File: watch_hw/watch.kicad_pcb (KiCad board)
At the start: 4 copper layers, 39 x 39.6 mm, 78 parts, among them J1 USB_C_Receptacle_USB2.0, M1 VZ43FC1B5640005L, Q1 DMN65D8LFB, Q2 SSM6J501NU, SW1 TL6340AF160Q, SW2 TL6340AF160Q, U1 BLUENRG-LPS, U2 FT234XD-R, U3 MAX17048G+, U4 LTC3130EUDC-1#PBF, U5 MCP73831-2ACI/MC, U6 MAXM86161EFD+T, U7 BMA456, Y1 Crystal_Small, Y2 Crystal_Small

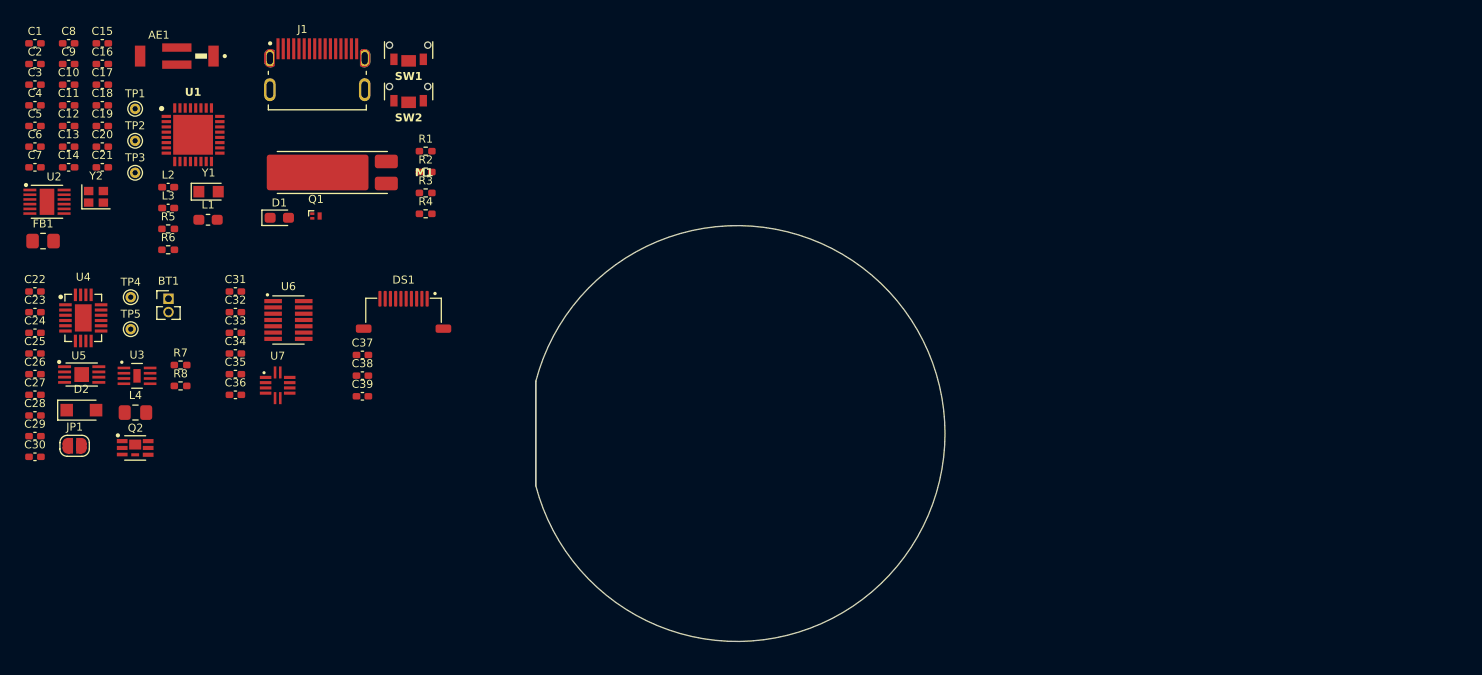
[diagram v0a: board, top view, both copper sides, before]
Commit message: Finalize (?) part selection, start layout
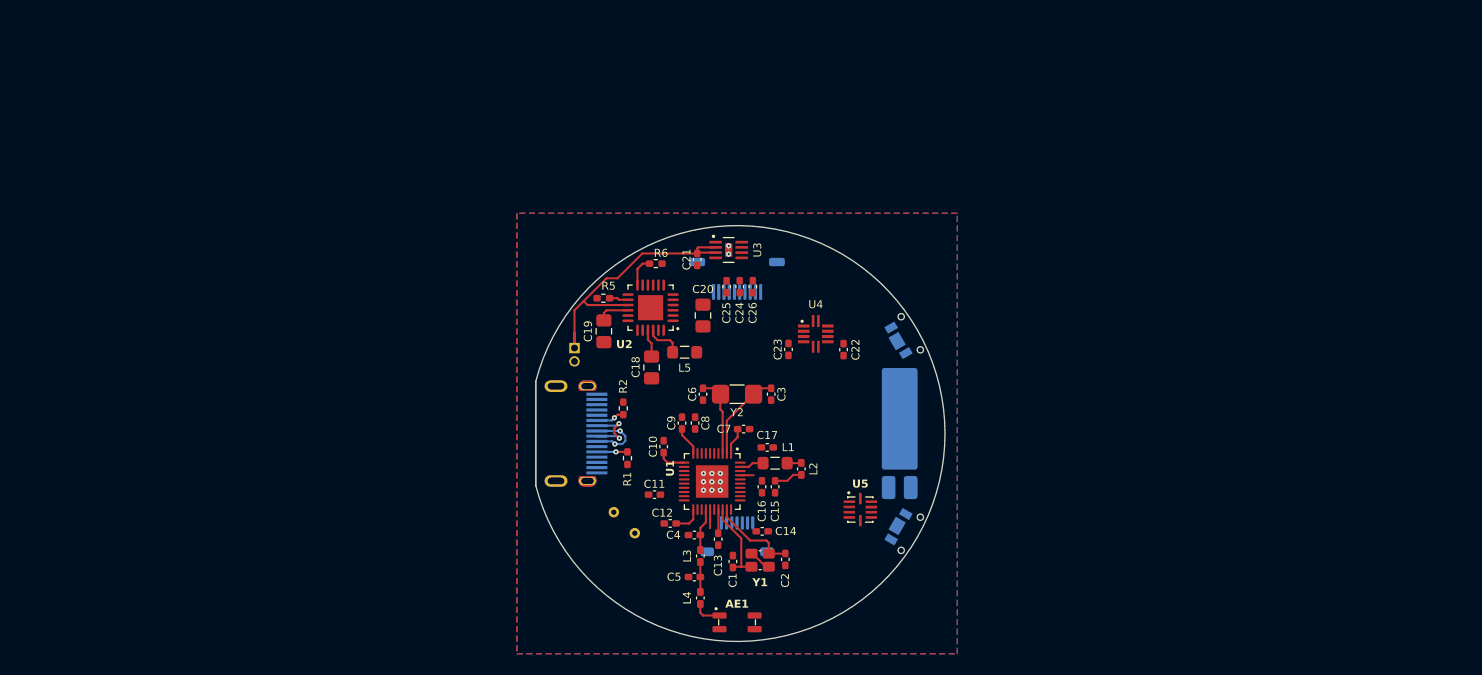
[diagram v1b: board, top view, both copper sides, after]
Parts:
- removed C27: 33u, Capacitor_SMD:C_0402_1005Metric_Pad0.74x0.62mm_HandSolder
- removed C28, C29, C30: 4.7u, Capacitor_SMD:C_0402_1005Metric_Pad0.74x0.62mm_HandSolder
- removed C31: 10u, Capacitor_SMD:C_0402_1005Metric_Pad0.74x0.62mm_HandSolder
- removed C32, C34, C35, C39: 0.1u, Capacitor_SMD:C_0402_1005Metric_Pad0.74x0.62mm_HandSolder
- removed C33, C36, C37, C38: 1u, Capacitor_SMD:C_0402_1005Metric_Pad0.74x0.62mm_HandSolder
- removed D1: D, Diode_SMD:D_0603_1608Metric_Pad1.05x0.95mm_HandSolder
- removed D2: PMEG10020AELR, Diode_SMD:Nexperia_CFP3_SOD-123W
- removed FB1: MI0805K601R-10, Resistor_SMD:R_0805_2012Metric_Pad1.20x1.40mm_HandSolder
- removed JP1: SolderJumper_2_Open, Jumper:SolderJumper-2_P1.3mm_Open_RoundedPad1.0x1.5mm
- removed Q1: DMN65D8LFB, Package_DFN_QFN:Diodes_DFN1006-3
- removed Q2: SSM6J501NU, watch:TRANS_SSM6J501NU,LF
- removed R3: 220, Resistor_SMD:R_0402_1005Metric_Pad0.72x0.64mm_HandSolder
- removed R4, R7: 10k, Resistor_SMD:R_0402_1005Metric_Pad0.72x0.64mm_HandSolder
- removed R8: 5k, Resistor_SMD:R_0402_1005Metric_Pad0.72x0.64mm_HandSolder
- removed TP3: SWDIO, TestPoint:TestPoint_THTPad_D1.0mm_Drill0.5mm
- removed TP4: VDD, TestPoint:TestPoint_THTPad_D1.0mm_Drill0.5mm
- removed TP5: PGOOD, TestPoint:TestPoint_THTPad_D1.0mm_Drill0.5mm
- removed U6: MAXM86161EFD+T, watch:MAXM86161EFDT
- removed U7: BMA456, watch:XDCR_BMA456
- added J2: FH19C-7S-0.5SH, watch:FH19C-7S-0.5SH, B.Cu at (140.0, 110.0)
- added L5: 2.2uH, Inductor_SMD:L_0805_2012Metric_Pad1.05x1.20mm_HandSolder, F.Cu at (135.0, 92.2)
- AE1: value 2450AT43B100E -> 2450AT18D0100001; footprint watch:ANTENNA_2450AT43B100E -> watch:ANTENNA_2450AT18D0100001
- BT1: value Battery_Cell -> 402530; moved to B.Cu
- C1, C2: value 200nF -> 9pF
- C11: value 4.7uF -> 100nF
- C12: value 100nF -> 820pF
- C13: value 10nF -> 100pF
- C14: value 47pF -> 100nF
- C15: value 47pF -> 1uF
- C16: value 100nF -> 47nF
- C17: value 8.2pF -> 1uF
- C18, C19, C20: value 8.2pF -> 10uF; footprint Capacitor_SMD:C_0402_1005Metric_Pad0.74x0.62mm_HandSolder -> Capacitor_SMD:C_0805_2012Metric_Pad1.18x1.45mm_HandSolder
- C21: value 8.2pF -> 0.1u
- C23: value 22n -> 0.1u
- C24: value 22n -> 1u
- C25: value 47u -> 1u
- C26: value 1uF -> 0.1u
- C3, C6: value 200nF -> 10pF
- C4: value 200nF -> 1pF
- C5: value 200nF -> 1.2pF
- C7: value 200nF -> 100nF
- C8: value 200nF -> 4.7uF
- C9: value 100nF -> 4.7uF
- DS1, J1, M1, SW1, SW2: moved to B.Cu
- L1: footprint Inductor_SMD:L_0603_1608Metric_Pad1.05x0.95mm_HandSolder -> Inductor_SMD:L_0805_2012Metric_Pad1.05x1.20mm_HandSolder
- L2: value 22nH -> 15nH
- L3: value 22nH -> 4.7nF
- L4: value 4.7u -> 2.2nH; footprint Inductor_SMD:L_0805_2012Metric_Pad1.15x1.40mm_HandSolder -> Inductor_SMD:L_0402_1005Metric_Pad0.77x0.64mm_HandSolder
- R5: value 27R -> 10k
- R6: value 27R -> 560R
- TP1: value ~{RESET} -> SWDCLK; moved to B.Cu
- TP2: value SWDCLK -> SWDIO; moved to B.Cu
- U1: value BLUENRG-LPS -> NRF52833-QDAA; footprint watch:BLUERNG-332 -> watch:nRF52833-QD
- U2: value FT234XD-R -> nPM1100-QD; footprint watch:SON45P300X300X80-13N -> watch:nPM1100-QD
- U4: value LTC3130EUDC-1#PBF -> BMA456; footprint watch:QFN50P300X400X80-21M-D -> watch:XDCR_BMA456
- U5: value MCP73831-2ACI/MC -> DRV2603; footprint watch:SON50P200X300X100-9N -> watch:DRV2603RUN
- Y1: value Crystal_Small -> 32MHz; footprint Crystal:Crystal_SMD_2012-2Pin_2.0x1.2mm_HandSoldering -> watch:XTAL_ECX-1637B2
- Y2: value Crystal_Small -> 32.768kHz; footprint Crystal:Crystal_SMD_2016-4Pin_2.0x1.6mm -> watch:XTAL_SC32S
- moved C2 85.7 mm to (144.6, 112.0), turned to 90 degrees
- moved C1 82.9 mm to (139.6, 112.2), turned to -90 degrees
- moved C22 77.3 mm to (150.1, 92.0), turned to -90 degrees
- moved C15 76.8 mm to (143.6, 105.1), turned to -90 degrees
- moved C5 76.2 mm to (135.9, 113.7), turned to 180 degrees
- moved C3 76.1 mm to (143.2, 96.2), turned to 90 degrees
- moved AE1 75.9 mm to (140.0, 118.0)
- moved U5 75.3 mm to (151.7, 107.2)
- moved C4 75.0 mm to (135.9, 109.7), turned to 180 degrees
- moved C16 74.7 mm to (142.3, 105.1), turned to -90 degrees
- moved C14 74.7 mm to (142.4, 109.3)
- moved C13 72.4 mm to (138.2, 110.1), turned to -90 degrees
- moved C17 72.2 mm to (142.8, 101.3)
- moved C7 72.0 mm to (140.6, 99.6)
- moved C23 71.9 mm to (144.9, 92.0), turned to -90 degrees
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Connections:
- net /BLUENRG/DISP_INVERT renamed /Display/INVERT
- net /BLUENRG/DISP_SCLK renamed /Display/SCLK
- net /BLUENRG/DISP_SDO renamed /Display/SDI
- net /BLUENRG/TXD renamed /Power/BAT_ERR
- net /BLUENRG/~{BAT_ALRT} renamed /Power/~{BAT_ALRT}
- net /BLUENRG/~{CTS} renamed /Power/BAT_CHG
- AE1 pad 1: Net-(AE1-A) -> Net-(AE1-FEED)
- AE1 pad 2: (no net) -> GND
- C1 pad 1: VDD -> GND
- C1 pad 2: GND -> Net-(U1-XC1)
- C10 pad 1: Net-(U1-VFBSD) -> /SoC/DECUSB
- C11 pad 1: Net-(U2-VCC) -> VDD
- C12 pad 1: Net-(U2-VCC) -> /SoC/DEC5
- C13 pad 1: VBUS -> /SoC/DEC3
- C14 pad 1: GND -> VDD
- C14 pad 2: /BLUENRG/D_P -> GND
- C15 pad 1: GND -> /SoC/DEC6
- C15 pad 2: /BLUENRG/D_N -> GND
- C16 pad 1: /BLUENRG/USB_3V3 -> /SoC/DEC6
- C17 pad 1: Net-(U1-AT3/PB12/XTALO) -> VDD
- C18 pad 1: Net-(U1-AT2/PB13/XTALI) -> Net-(U2-DEC)
- C19 pad 1: Net-(U1-RF1) -> /Power/VSYS
- C19 pad 2: Net-(AE1-A) -> GND
- C2 pad 1: VDD -> GND
- C2 pad 2: GND -> Net-(U1-XC2)
- C20 pad 1: Net-(U1-RF1) -> VDD
- C21 pad 1: Net-(AE1-A) -> /Power/VBAT
- C22 pad 1: /Power/VBAT -> VDD
- C23 pad 1: Net-(U4-SW1) -> VDD
- C23 pad 2: Net-(U4-BST1) -> GND
- C24 pad 1: Net-(U4-BST2) -> VDD
- C24 pad 2: Net-(U4-SW2) -> GND
- C25 pad 1: Net-(D2-K) -> VDD
- C26 pad 1: Net-(D2-K) -> /Display/DISP_ON
- C3 pad 1: VDD -> GND
- C3 pad 2: GND -> Net-(U1-P0.00/XL1)
- C4 pad 1: VDD -> Net-(U1-ANT)
- C5 pad 1: VDD -> Net-(C5-Pad1)
- C6 pad 1: VDD -> GND
- C6 pad 2: GND -> Net-(U1-P0.01/XL2)
- C7 pad 1: /BLUENRG/VCAP -> /SoC/DEC1
- C9 pad 1: Net-(U1-VFBSD) -> VBUS
- DS1 pad 5: /BLUENRG/DISP_ON -> /Display/DISP_ON
- J1 pad A6: /BLUENRG/D_P -> /USB_D_P
- J1 pad A7: /BLUENRG/D_N -> /USB_D_N
- J1 pad B6: /BLUENRG/D_P -> /USB_D_P
- J1 pad B7: /BLUENRG/D_N -> /USB_D_N
- L1 pad 1: Net-(U1-VFBSD) -> Net-(U1-DCC)
- L2 pad 2: Net-(U1-VLXSD) -> /SoC/DEC6
- L3 pad 1: Net-(U1-RF1) -> Net-(U1-ANT)
- L3 pad 2: Net-(AE1-A) -> Net-(C5-Pad1)
- L4 pad 1: Net-(U4-SW1) -> Net-(C5-Pad1)
- L4 pad 2: Net-(U4-SW2) -> Net-(AE1-FEED)
- M1 pad 1: VDD -> Net-(M1-+)
- M1 pad 2: Net-(D1-A) -> Net-(M1--)
- R5 pad 1: Net-(U2-USBDM) -> GND
- R5 pad 2: /BLUENRG/D_N -> Net-(U2-NTC)
- R6 pad 1: Net-(U2-USBDP) -> GND
- R6 pad 2: /BLUENRG/D_P -> Net-(U2-ICHG)
- TP1 pad 1: Net-(U1-RSTN) -> Net-(U1-SWDCLK)
- TP2 pad 1: Net-(U1-PA3) -> Net-(U1-SWDIO)
- U1 pad 1: unconnected-(U1-PB3-Pad1) -> /SoC/DEC1
- U1 pad 10: unconnected-(U1-PA9-Pad10) -> VBUS
- U1 pad 11: unconnected-(U1-PA10-Pad11) -> /SoC/DECUSB
- U1 pad 12: unconnected-(U1-PA11-Pad12) -> /USB_D_N
- U1 pad 13: VDD -> /USB_D_P
- U1 pad 14: Net-(U1-RF1) -> unconnected-(U1-P0.15-Pad14)
- U1 pad 15: VDD -> unconnected-(U1-P0.17-Pad15)
- U1 pad 16: Net-(U1-OSCOUT) -> unconnected-(U1-P0.18/~{RESET}-Pad16)
- U1 pad 17: Net-(U1-OSCIN) -> unconnected-(U1-P0.20-Pad17)
- U1 pad 18: unconnected-(U1-AT0/PB15-Pad18) -> VDD
- U1 pad 19: unconnected-(U1-AT1/PB14-Pad19) -> Net-(U1-SWDIO)
- U1 pad 2: unconnected-(U1-PB2-Pad2) -> Net-(U1-P0.00/XL1)
- U1 pad 20: Net-(U1-AT2/PB13/XTALI) -> Net-(U1-SWDCLK)
- U1 pad 21: Net-(U1-AT3/PB12/XTALO) -> /SoC/DEC5
- U1 pad 24: VDD -> Net-(U1-ANT)
- U1 pad 25: Net-(U1-VLXSD) -> GND
- U1 pad 26: GND -> /SoC/DEC6
- U1 pad 27: Net-(U1-VFBSD) -> /SoC/DEC3
- U1 pad 28: /BLUENRG/VCAP -> Net-(U1-XC1)
- U1 pad 29: Net-(U1-RSTN) -> Net-(U1-XC2)
- U1 pad 3: unconnected-(U1-PB1-Pad3) -> Net-(U1-P0.01/XL2)
- U1 pad 30: unconnected-(U1-PB5-Pad30) -> VDD
- U1 pad 32: VDD -> unconnected-(U1-P0.02/AIN0-Pad32)
- U1 pad 33: GND -> unconnected-(U1-P0.28/AIN4-Pad33)
- U1 pad 5: Net-(U1-PA3) -> unconnected-(U1-P0.05/AIN3-Pad5)
- U1 pad 6: Net-(U1-PA2) -> unconnected-(U1-P1.09-Pad6)
- U1 pad 8: unconnected-(U1-PA0-Pad8) -> VDD
- U1 pad 9: unconnected-(U1-PA8-Pad9) -> VDD
- U2 pad 1: Net-(U2-USBDM) -> VDD
- U2 pad 11: /BLUENRG/~{RTS} -> GND
- U2 pad 12: Net-(U2-USBDP) -> Net-(U2-ICHG)
- U2 pad 13: GND -> unconnected-(U2-NC-Pad13)
- U2 pad 2: /BLUENRG/USB_3V3 -> /Power/VSYS
- U2 pad 3: /BLUENRG/USB_3V3 -> /Power/VSYS
- U2 pad 4: Net-(U2-VCC) -> unconnected-(U2-NC-Pad4)
- U2 pad 5: GND -> /Power/VSYS
- U2 pad 6: unconnected-(U2-CBUS0-Pad6) -> GND
- U2 pad 7: /BLUENRG/RXD -> GND
- U2 pad 9: /BLUENRG/USB_3V3 -> /Power/VSYS
- U4 pad 1: Net-(U4-BST1) -> GND
- U4 pad 10: /Power/BOOST_VCC -> VDD
- U4 pad 11: GND -> unconnected-(U4-ASCL-Pad11)
- U4 pad 12: Net-(JP1-A) -> /SCL
- U4 pad 2: Net-(D2-K) -> /SDA
- U4 pad 3: Net-(D2-K) -> VDD
- U4 pad 4: Net-(D2-K) -> unconnected-(U4-ASDA-Pad4)
- U4 pad 5: /Power/BOOST_VCC -> /Sensors/ACC_INT1
- U4 pad 6: /Power/BOOST_VCC -> /Sensors/ACC_INT2
- U4 pad 7: GND -> VDD
- U5 pad 1: VBUS -> /MOTOR_EN
- U5 pad 2: VBUS -> /MOTOR_PWM
- U5 pad 3: /Power/VBAT -> GND
- U5 pad 4: /Power/VBAT -> (no net)
- U5 pad 5: /Power/STAT -> GND
- U5 pad 6: GND -> Net-(M1--)
- U5 pad 7: (no net) -> VDD
- U5 pad 8: Net-(U5-PROG) -> GND
- U5 pad 9: GND -> Net-(M1-+)
- Y1 pad 1: Net-(U1-AT2/PB13/XTALI) -> Net-(U1-XC1)
- Y1 pad 2: Net-(U1-AT3/PB12/XTALO) -> GND
- Y2 pad 1: Net-(U1-OSCOUT) -> Net-(U1-P0.01/XL2)
- Y2 pad 2: Net-(U1-OSCIN) -> Net-(U1-P0.00/XL1)
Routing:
- net /Power/VBAT: track 0.00 -> 27.6 mm
- net Net-(U1-P0.00/XL1): track 0.00 -> 8.63 mm
- net Net-(U1-XC2): track 0.00 -> 8.35 mm
- net Net-(U1-XC1): track 0.00 -> 7.99 mm
- net Net-(U1-P0.01/XL2): track 0.00 -> 7.66 mm
- net /USB_D_P: track 0.00 -> 6.32 mm, vias 0 -> 2
- net /USB_D_N: track 0.00 -> 6.18 mm, vias 0 -> 2
- net GND: track 0.00 -> 5.20 mm, vias 0 -> 11
- net Net-(U1-ANT): track 0.00 -> 4.07 mm
- net Net-(U2-SW): track 0.00 -> 3.56 mm
- net /Power/VSYS: track 0.00 -> 3.12 mm
- net Net-(J1-CC1): track 0.00 -> 2.91 mm, vias 0 -> 1
- net Net-(U2-ICHG): track 0.00 -> 2.91 mm
- net Net-(C5-Pad1): track 0.00 -> 2.86 mm
- net VBUS: track 0.00 -> 2.78 mm
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- added copper zone on B.Cu, net GND
- added copper zone on F.Cu, net GND
- added copper zone on In1.Cu, net GND
- added copper zone on In4.Cu, net GND
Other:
- copper layers 4 -> 6

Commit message: Routing progress
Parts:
- added TP3: RESET, TestPoint:TestPoint_THTPad_D1.0mm_Drill0.5mm, B.Cu at (127.8, 106.2)
- C26: value 0.1u -> 0.1uF
- DS1: moved to F.Cu
- moved C26 25.1 mm to (154.3, 107.6), turned to -90 degrees
- moved DS1 22.8 mm to (155.8, 100.0), turned to 90 degrees
- moved C25 18.3 mm to (149.4, 101.0), turned to 180 degrees
- moved C24 16.5 mm to (149.4, 99.8), turned to 180 degrees
- moved AE1 13.7 mm to (127.5, 112.5), turned to 135 degrees
- moved J2 7.00 mm to (140.0, 117.0)
- moved L4 2.78 mm to (134.5, 113.8), turned to 180 degrees
- moved C15 2.67 mm to (146.2, 105.8)
- moved C16 2.67 mm to (144.9, 105.8)
- moved C14 1.64 mm to (142.6, 107.7)
- moved C1 1.60 mm to (139.4, 110.6)
- moved C2 1.58 mm to (144.4, 110.4)
- moved Y1 1.58 mm to (142.0, 110.5)
- moved TP2 1.25 mm to (129.2, 108.2)
- moved C13 1.18 mm to (138.2, 111.2)
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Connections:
- C26 pad 1: /Display/DISP_ON -> VDD
- DS1 pad 3: VDD -> /Display/DISP_CS
- DS1 pad 4: /Display/INVERT -> GND
- DS1 pad 5: /Display/DISP_ON -> VDD
- DS1 pad 8: unconnected-(DS1-EXTMODE-Pad8) -> GND
- J2 pad 3: /Sensors/HR_GPIO -> unconnected-(J2-Pin_3-Pad3)
- J2 pad 4: /Sensors/HR_LDO_EN -> unconnected-(J2-Pin_4-Pad4)
- U1 pad 16: unconnected-(U1-P0.18/~{RESET}-Pad16) -> Net-(U1-P0.18/~{RESET})
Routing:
- net VDD: track 0.00 -> 33.8 mm, vias 0 -> 11
- net /USB_D_P: track 6.32 -> 23.4 mm
- net /USB_D_N: track 6.18 -> 22.5 mm
- net GND: track 5.20 -> 14.8 mm, vias 11 -> 18
- net Net-(U1-P0.18/~{RESET}): track 0.00 -> 7.71 mm
- net Net-(U1-SWDIO): track 0.00 -> 6.64 mm
- net Net-(M1--): track 0.00 -> 6.45 mm, vias 0 -> 1
- net Net-(U1-SWDCLK): track 0.00 -> 6.05 mm
- net /Power/VSYS: track 3.12 -> 6.92 mm, vias 0 -> 5
- net /SoC/DEC6: track 2.73 -> 5.28 mm, vias 0 -> 2
- net /Power/VBAT: track 27.6 -> 25.3 mm
- net Net-(AE1-FEED): track 2.35 -> 4.48 mm
- net Net-(M1-+): track 0.00 -> 2.03 mm, vias 0 -> 1
- net Net-(U1-XC1): track 7.99 -> 6.32 mm
- net Net-(U1-XC2): track 8.35 -> 6.98 mm
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
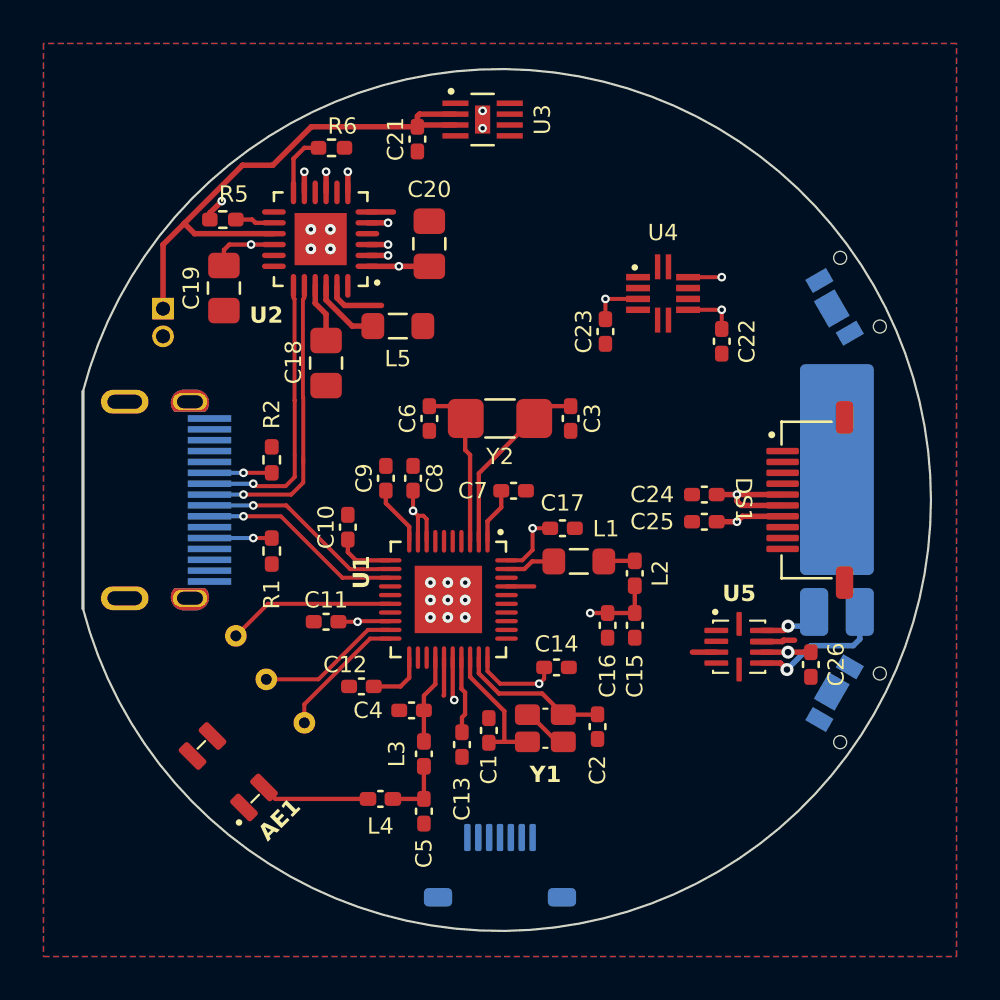
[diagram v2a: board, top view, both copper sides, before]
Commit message: Clean up library symbols, update to kicad 8
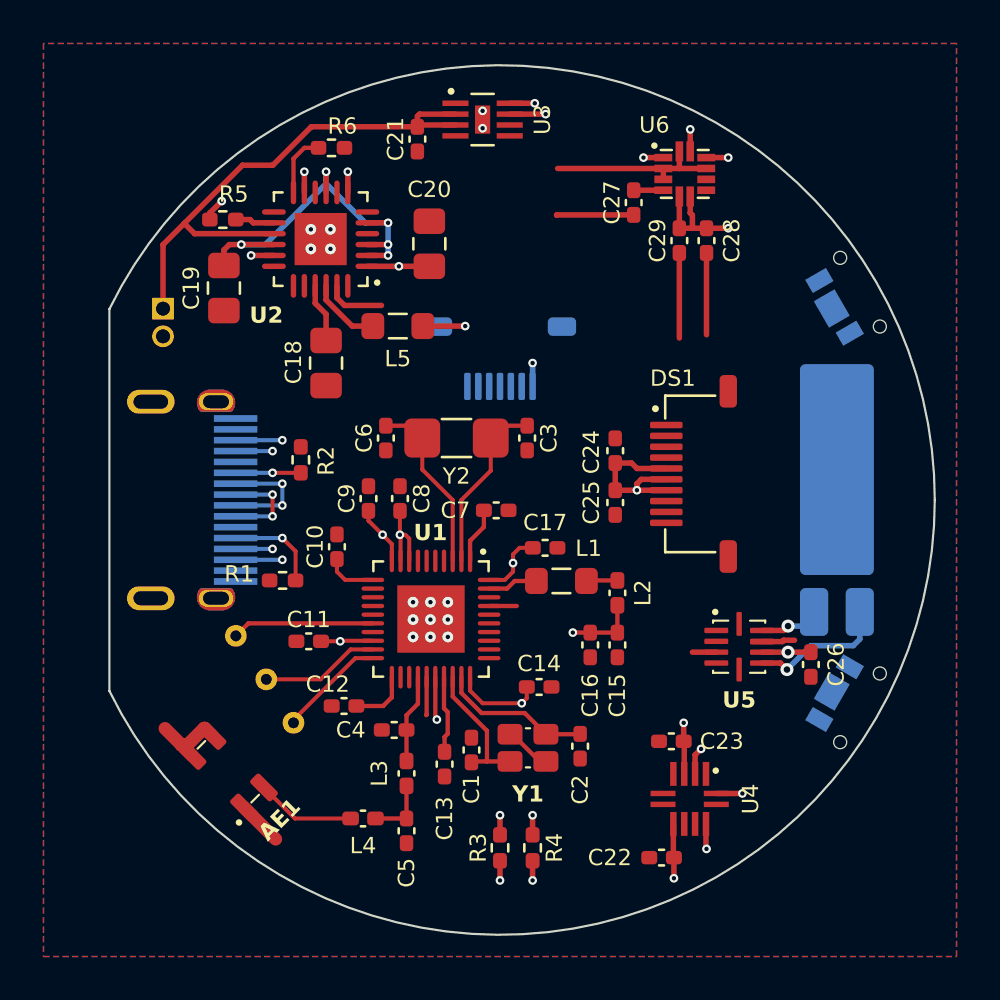
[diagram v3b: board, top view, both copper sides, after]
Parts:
- added C27: 0.1uF, Capacitor_SMD:C_0402_1005Metric_Pad0.74x0.62mm_HandSolder, F.Cu at (146.1, 86.3)
- added C28: 1uF, Capacitor_SMD:C_0402_1005Metric_Pad0.74x0.62mm_HandSolder, F.Cu at (149.5, 88.1)
- added C29: 0.1uF, Capacitor_SMD:C_0402_1005Metric_Pad0.74x0.62mm_HandSolder, F.Cu at (148.2, 88.1)
- added R3: 4.7k, Resistor_SMD:R_0402_1005Metric_Pad0.72x0.64mm_HandSolder, F.Cu at (140.0, 116.0)
- added R4: 4.7k, Resistor_SMD:R_0402_1005Metric_Pad0.72x0.64mm_HandSolder, F.Cu at (141.5, 116.0)
- added REF**: LS012B7DH02, watch:LS012B7DH02, F.Cu at (140.0, 100.0)
- added REF**: BATT_402530, watch:BATT_402530, B.Cu at (140.0, 100.0)
- added U6: LIS3MDL, watch:LIS3MDLTR, F.Cu at (148.5, 85.0)
- C11, C14, C7: value 100nF -> 0.1uF
- C21, C22, C23: value 0.1u -> 0.1uF
- C24, C25: value 1u -> 1uF
- J1: value USB_C_Receptacle_USB2.0 -> 2130830005
- moved C22 23.9 mm to (147.4, 116.5), turned to 180 degrees
- moved J2 23.7 mm to (140.0, 93.3), turned to 0 degrees
- moved U4 23.3 mm to (148.7, 113.8), turned to -90 degrees
- moved C23 19.1 mm to (147.8, 111.1), turned to 180 degrees
- moved DS1 5.48 mm to (150.5, 98.8)
- moved C24 4.57 mm to (145.3, 97.7), turned to 90 degrees
- moved C25 4.19 mm to (145.3, 100.1), turned to -90 degrees
- moved C3 2.19 mm to (141.2, 97.2)
- moved C6 2.19 mm to (134.7, 97.2)
- moved Y2 2.19 mm to (138.0, 97.2)
- moved R1 1.44 mm to (130.0, 103.7), turned to 180 degrees
- moved R2 1.34 mm to (130.8, 98.2)
- moved C9 1.23 mm to (133.9, 99.9)
- moved C1 1.20 mm to (138.6, 111.5)
- moved C11 1.20 mm to (131.2, 106.5)
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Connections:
- net /Sensors/ACC_INT1 renamed /Sensors/ACC_INT
- J1 pad SH1: (no net) -> GND
- J1 pad SH2: (no net) -> GND
- J1 pad SH3: (no net) -> GND
- J1 pad SH4: (no net) -> GND
- J2 pad 2: /Sensors/HR_INT -> unconnected-(J2-Pin_2-Pad2)
- U4 pad 6: /Sensors/ACC_INT2 -> unconnected-(U4-INT2-Pad6)
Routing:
- net GND: track 14.8 -> 38.7 mm
- net /USB_D_P: track 23.4 -> 4.12 mm
- net /USB_D_N: track 22.5 -> 5.02 mm
- net VDD: track 33.8 -> 50.3 mm, vias 11 -> 16
- net /Power/VSYS: track 6.92 -> 17.6 mm
- net VBUS: track 2.78 -> 10.9 mm, vias 0 -> 6
- net /SoC/DEC6: track 5.28 -> 13.2 mm
- net /SCL: track 0.00 -> 4.67 mm, vias 0 -> 4
- net /SDA: track 0.00 -> 4.33 mm, vias 0 -> 4
- net Net-(U6-C1): track 0.00 -> 1.36 mm
- net Net-(J1-CC1): track 2.91 -> 4.22 mm
- net Net-(U1-SWDIO): track 6.64 -> 5.47 mm
- net Net-(U1-P0.18/~{RESET}): track 7.71 -> 6.54 mm
- net Net-(U1-SWDCLK): track 6.05 -> 4.96 mm
- net Net-(U1-P0.00/XL1): track 8.63 -> 8.12 mm
- added copper zone on In2.Cu, net VBUS
- added copper zone on In2.Cu, net VDD
- added copper zone on In3.Cu, net VDD
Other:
- board size 39 x 39.6 mm -> 38 x 40 mm
